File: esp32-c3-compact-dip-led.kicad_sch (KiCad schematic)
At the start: 29 parts, among them J1 PJ-102A compatible 5.5/2.1mm, J2 USB-C POWER ONLY, J3 LED OUT, J4 M5STACK A105, Q1 RJP020N06T100, U1 ESP32-C3-WROOM-02-N4, U2 LMR36510FADDAR

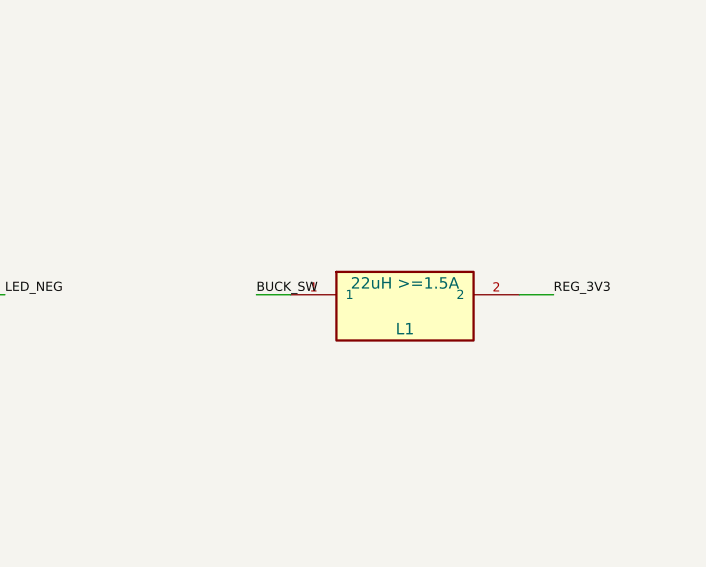
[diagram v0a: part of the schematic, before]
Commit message: Use lower-cost 2A buck inductor
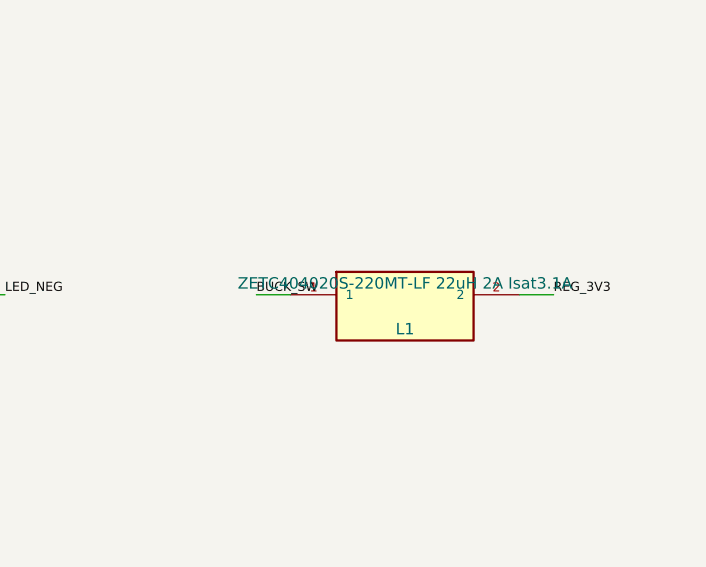
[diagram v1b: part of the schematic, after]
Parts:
- L1: value 22uH >=1.5A -> ZETC404020S-220MT-LF 22uH 2A Isat3.1A
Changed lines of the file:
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@@
 			)
 		)
-		(property "Value" "22uH >=1.5A"
+		(property "Value" "ZETC404020S-220MT-LF 22uH 2A Isat3.1A"
 			(at 330.2 76.2 0)
 			(effects
